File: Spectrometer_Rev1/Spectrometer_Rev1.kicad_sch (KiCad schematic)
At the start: 19 parts, among them J1 RJ45_LED_Shielded, U1 Teensy4.1_DEV-16771, U2 OKI

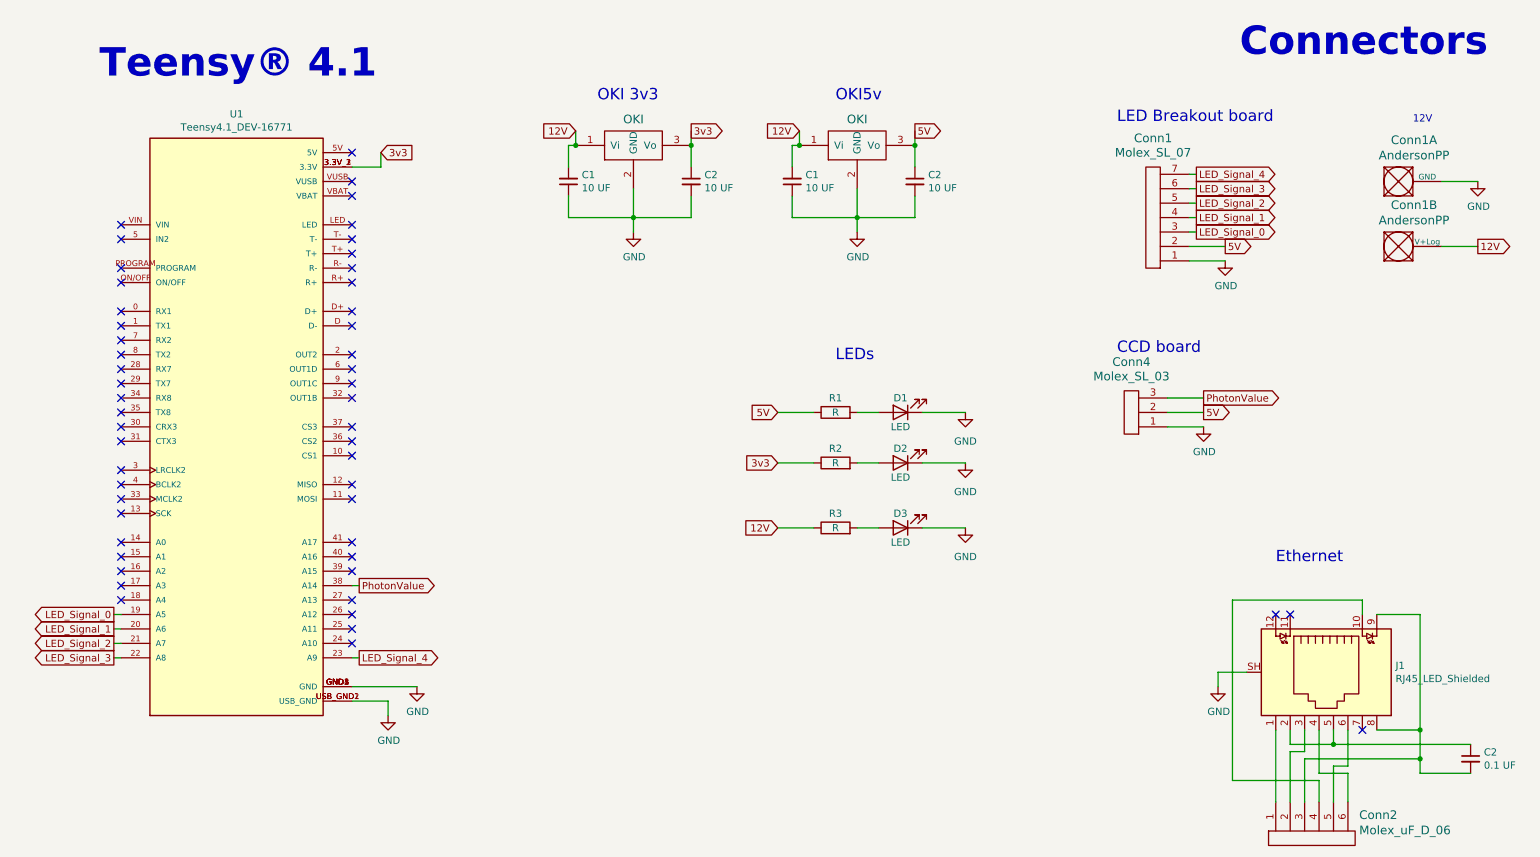
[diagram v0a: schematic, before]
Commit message: switch voltage symbols
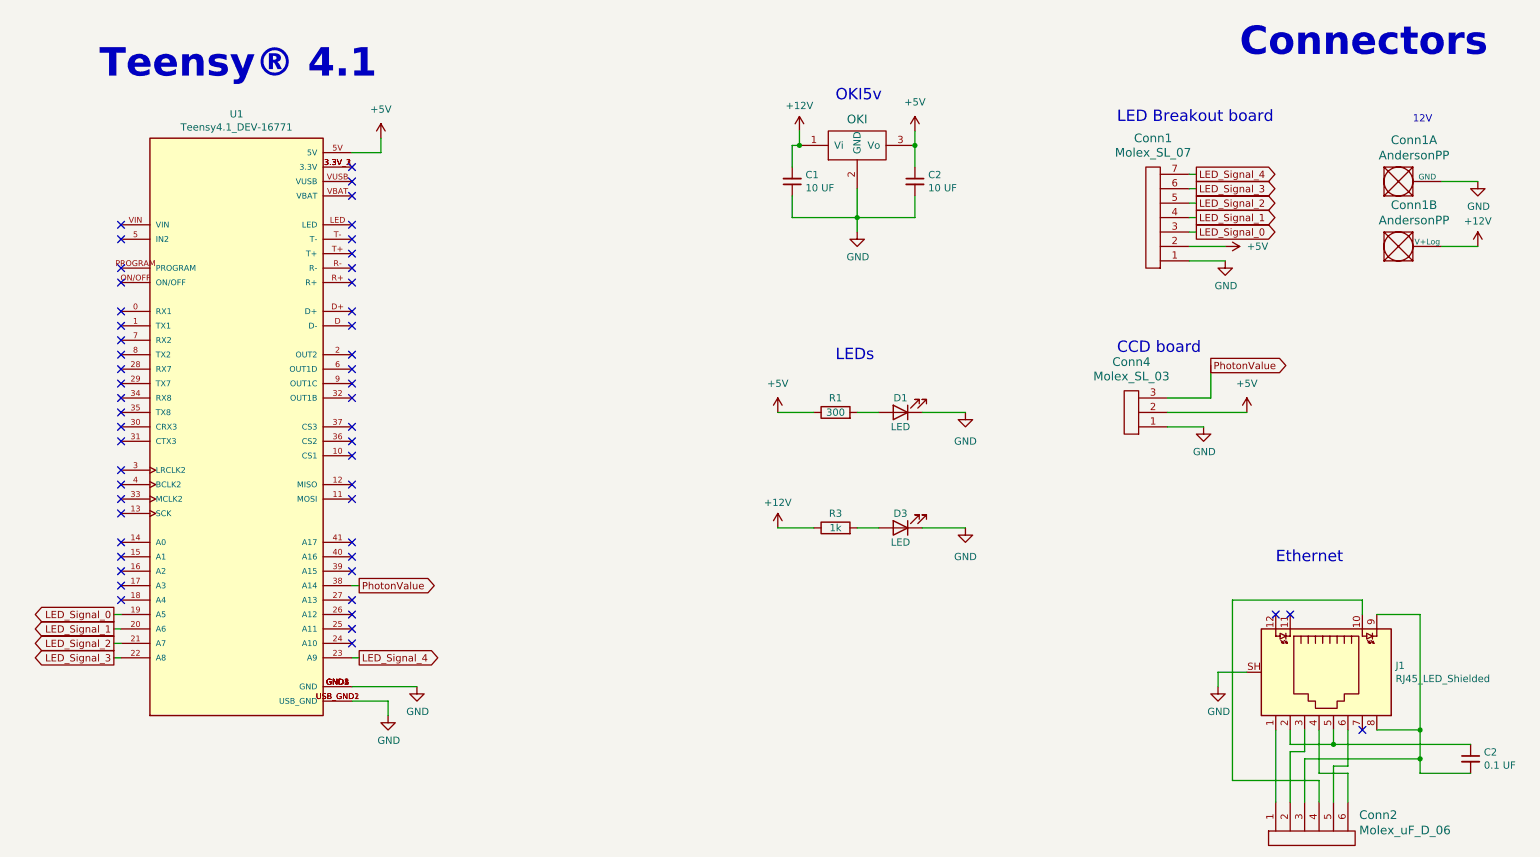
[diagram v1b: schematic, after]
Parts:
- removed C1, C2: 10 UF, Capacitor_SMD:C_0603_1608Metric_Pad1.08x0.95mm_HandSolder, symbol Device:C_Small
- removed D2: LED, symbol Device:LED
- removed R2: R, symbol Device:R
- removed U2: OKI, MRDT_Devices:OKI_Horizontal, symbol MRDT_Devices:OKI
- R1: value R -> 300
- R3: value R -> 1k
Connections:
- net 5V is gone; now on net +5V: C2.1, Conn1.2, Conn4.2, R1.1, U2.3 (Vo)
- net +5V: now reaches U1.5V
- net 12V renamed +12V
- net 3v3: no longer names the net of U1.3.3V_1 (3.3V), U1.3.3V_2 (3.3V), U1.3.3V_3 (3.3V)
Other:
- note removed: "OKI 3v3"

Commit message: import netlist for layout
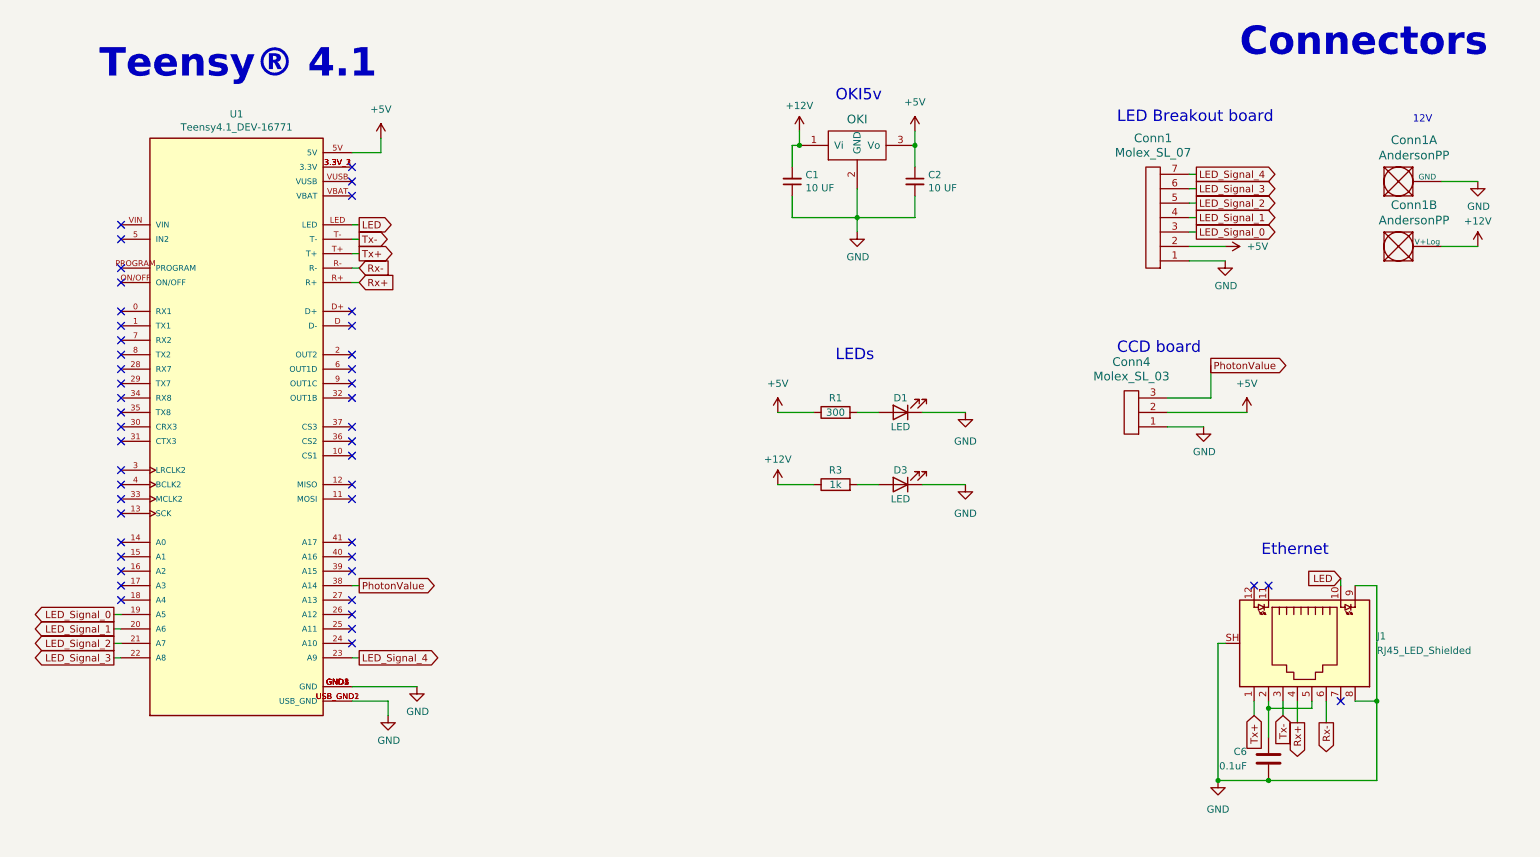
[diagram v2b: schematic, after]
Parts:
- removed C2: 0.1 UF, Capacitor_SMD:C_0603_1608Metric_Pad1.08x0.95mm_HandSolder, symbol Device:C_Small
- removed Conn2: Molex_uF_D_06, Connector_PinSocket_2.00mm:PinSocket_2x03_P2.00mm_Vertical, symbol MRDT_Connectors:Molex_uF_D_06
- added C6: 0.1uF, Capacitor_SMD:C_0603_1608Metric_Pad1.08x0.95mm_HandSolder, symbol Device:C
- Conn1: footprint (none) -> MRDT_Connectors:MOLEX_SL_07_Horizontal
- Conn4: footprint (none) -> MRDT_Connectors:MOLEX_SL_03_Horizontal
- D1, D3: footprint (none) -> LED_SMD:LED_0201_0603Metric_Pad0.64x0.40mm_HandSolder
- R1, R3: footprint (none) -> Resistor_SMD:R_0603_1608Metric_Pad0.98x0.95mm_HandSolder
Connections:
- net GND: now also J1.8, J1.9, C6.1
- net Tx+: now reaches J1.1
- net Tx+: now also U1.T+
- net LED: now reaches J1.10
- net LED: now also U1.LED
- net at J1.2, J1.5: now also C6.2
- net Tx-: now reaches J1.3
- net Tx-: now also U1.T-
- net Rx+: now reaches J1.4
- net Rx+: now also U1.R+
- net Rx-: now reaches J1.6
- net Rx-: now also U1.R-
- no-connect marks 52 -> 47
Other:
- moved on the sheet: D3, R3
